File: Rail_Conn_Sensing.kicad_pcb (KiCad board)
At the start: 2 copper layers, 29 parts, among them J1 Rail Sensing Inputs, J2 Vin & GND, J3 Outputs, U1 AMC1200, U2 AMC1200, U3 MCP6004, U4 74LS00, U5 74LS86, U6 L7805

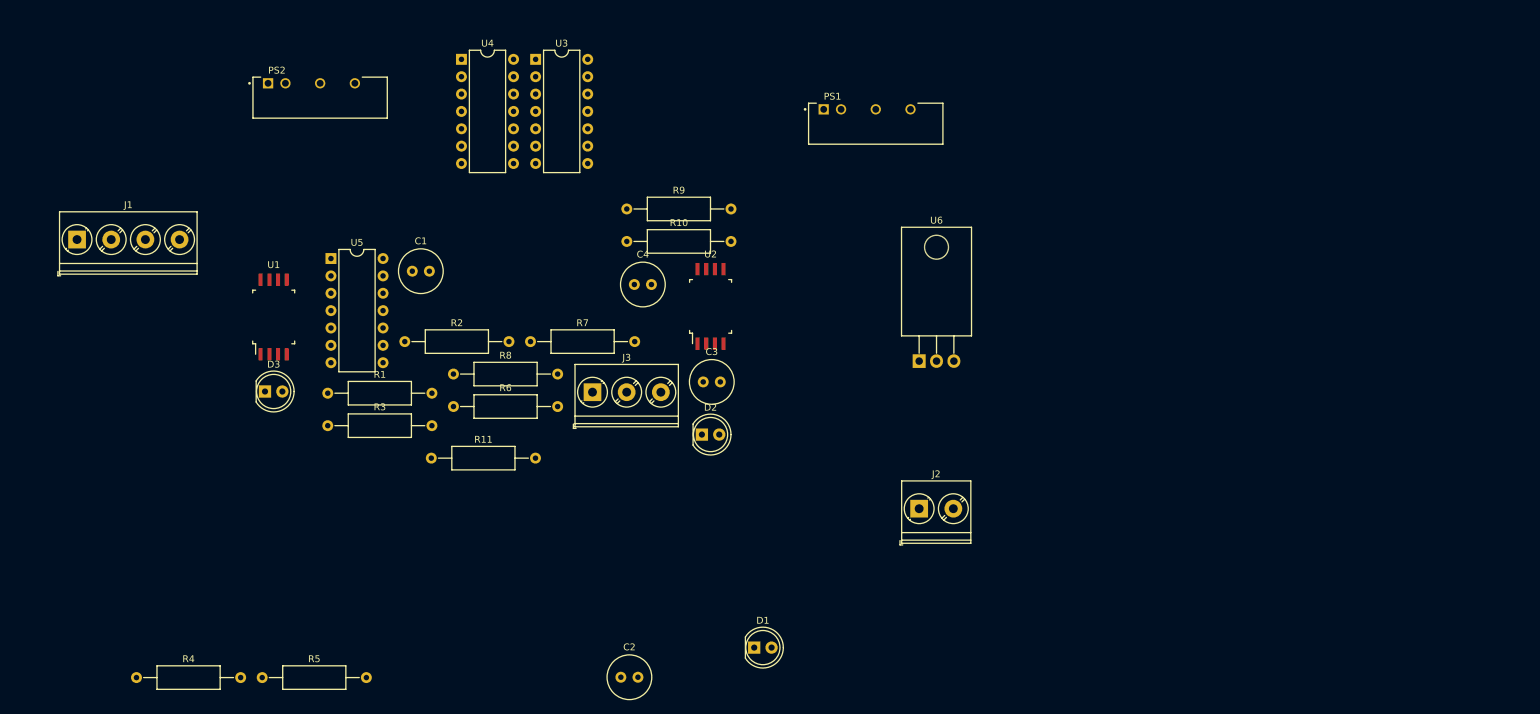
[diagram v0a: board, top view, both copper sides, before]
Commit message: Modified pcb layout
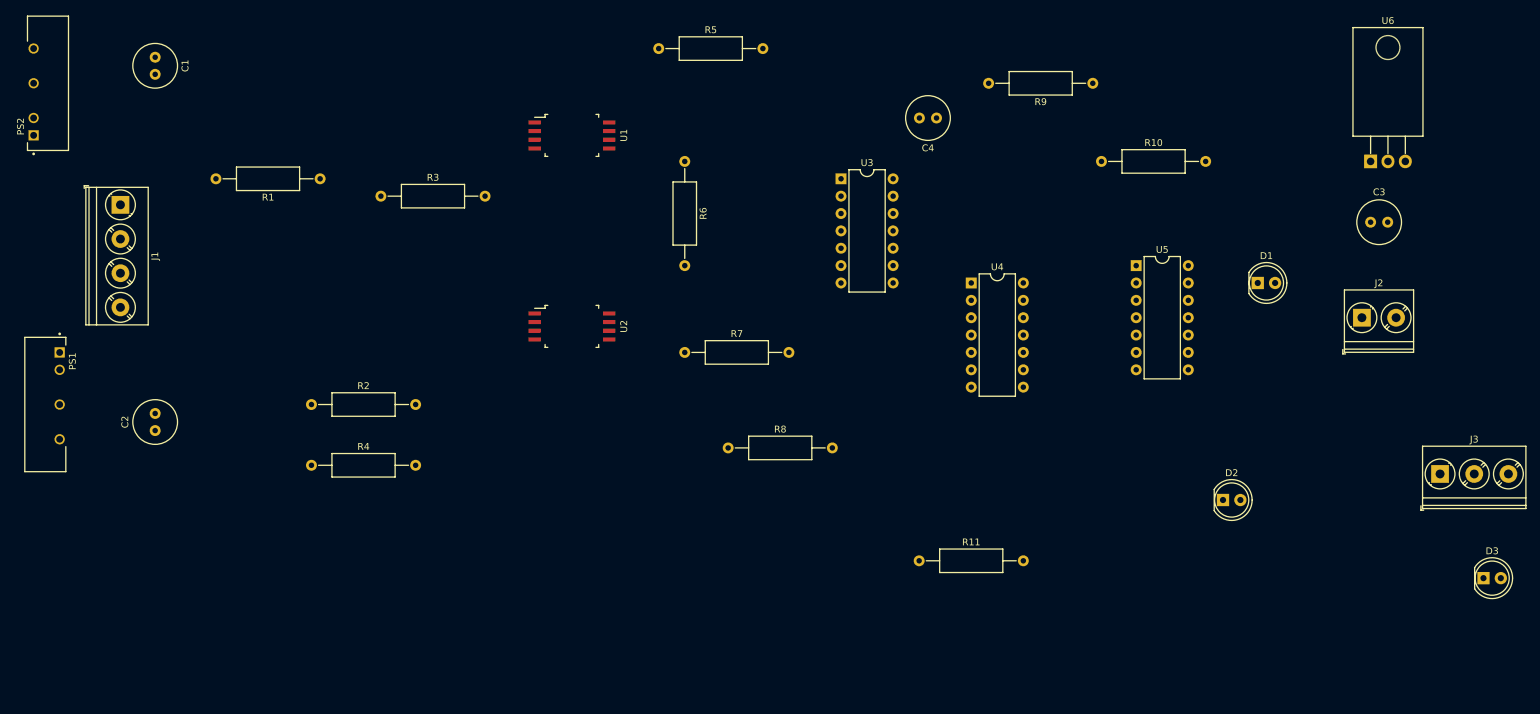
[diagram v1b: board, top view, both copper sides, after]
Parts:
- moved D3 180.3 mm to (227.3, 104.1)
- moved PS1 126.9 mm to (19.1, 78.7), turned to 270 degrees
- moved J3 124.6 mm to (221.0, 88.9)
- moved U5 117.8 mm to (176.5, 58.4)
- moved R5 108.8 mm to (106.7, 26.7)
- moved C3 100.4 mm to (210.8, 52.1)
- moved D1 90.9 mm to (194.3, 61.0)
- moved U4 81.4 mm to (152.4, 61.0)
- moved C2 77.1 mm to (33.0, 82.5), turned to 90 degrees
- moved D2 76.8 mm to (189.2, 92.7)
- moved R11 72.9 mm to (144.8, 101.6)
- moved U6 72.2 mm to (210.8, 43.2)
- moved R9 70.6 mm to (170.2, 31.8), turned to 180 degrees
- moved J2 70.5 mm to (209.6, 66.0)
- moved R10 70.4 mm to (171.4, 43.2)
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
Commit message: Modify placement of parts on PCB
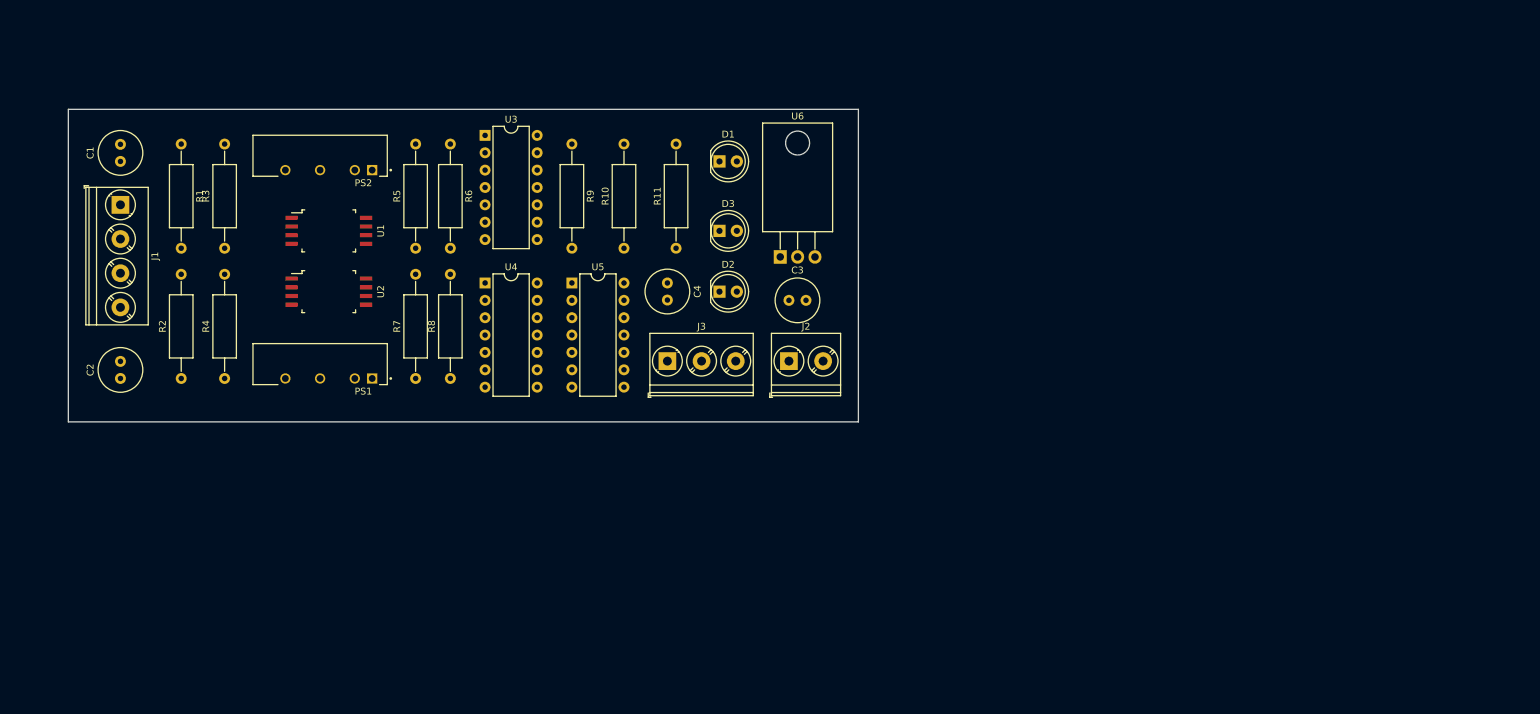
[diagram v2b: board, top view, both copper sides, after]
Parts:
- moved D3 122.8 mm to (115.6, 53.3)
- moved J3 114.2 mm to (108.0, 72.4)
- moved U6 87.5 mm to (124.5, 57.1)
- moved C3 85.9 mm to (125.7, 63.5)
- moved J2 84.1 mm to (125.7, 72.4)
- moved U5 82.6 mm to (94.0, 61.0)
- moved D1 80.7 mm to (115.6, 43.2)
- moved D2 79.7 mm to (115.6, 62.2)
- moved R9 76.7 mm to (94.0, 40.6), turned to 270 degrees
- moved U4 71.1 mm to (81.3, 61.0)
- moved R10 71.0 mm to (101.6, 55.9), turned to 90 degrees
- moved R11 57.9 mm to (109.2, 55.9), turned to 90 degrees
- moved U3 52.5 mm to (81.3, 39.4)
- moved C4 46.2 mm to (108.0, 61.0), turned to 270 degrees
- moved R5 46.0 mm to (71.1, 55.9), turned to 90 degrees
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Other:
- board outline added: 115.6 x 45.7 mm
- net class Default: clearance 0.2 -> 0.2032; trace_width 0.25 -> 0.2032; via_dia 0.8 -> 0.762; via_drill 0.4 -> 0.381
- net class Power added: clearance 0.3048, trace_width 0.3048, via_dia 0.762, via_drill 0.381
- rule pad_to_mask_clearance: 0.051 -> 0.0508
- rule solder_mask_min_width: 0.25 -> 0.1016
- rule trace_clearance: 0.2 -> 0.2032
- rule trace_min: 0.2 -> 0.2032
- rule via_min_drill: 0.3 -> 0.254
- rule via_min_size: 0.4 -> 0.508

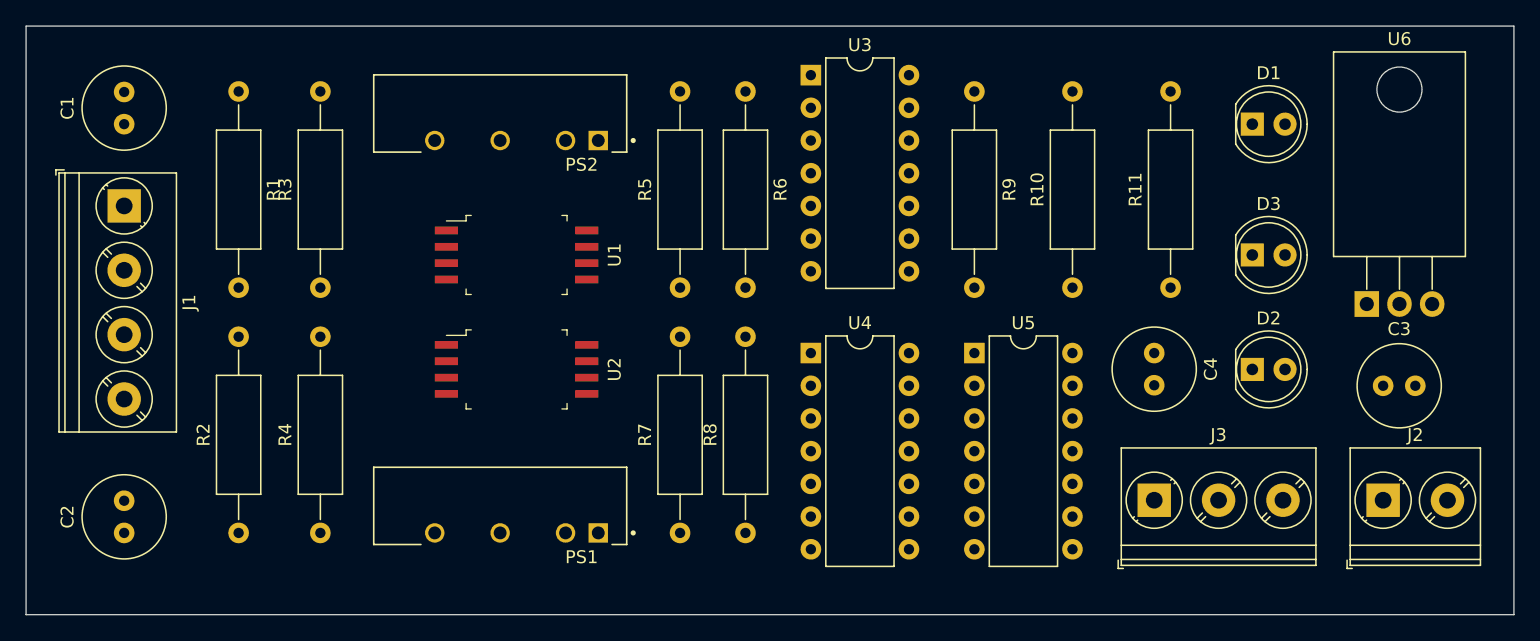
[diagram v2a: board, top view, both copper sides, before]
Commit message: Delete extra resistor divider and re-arrange pcb
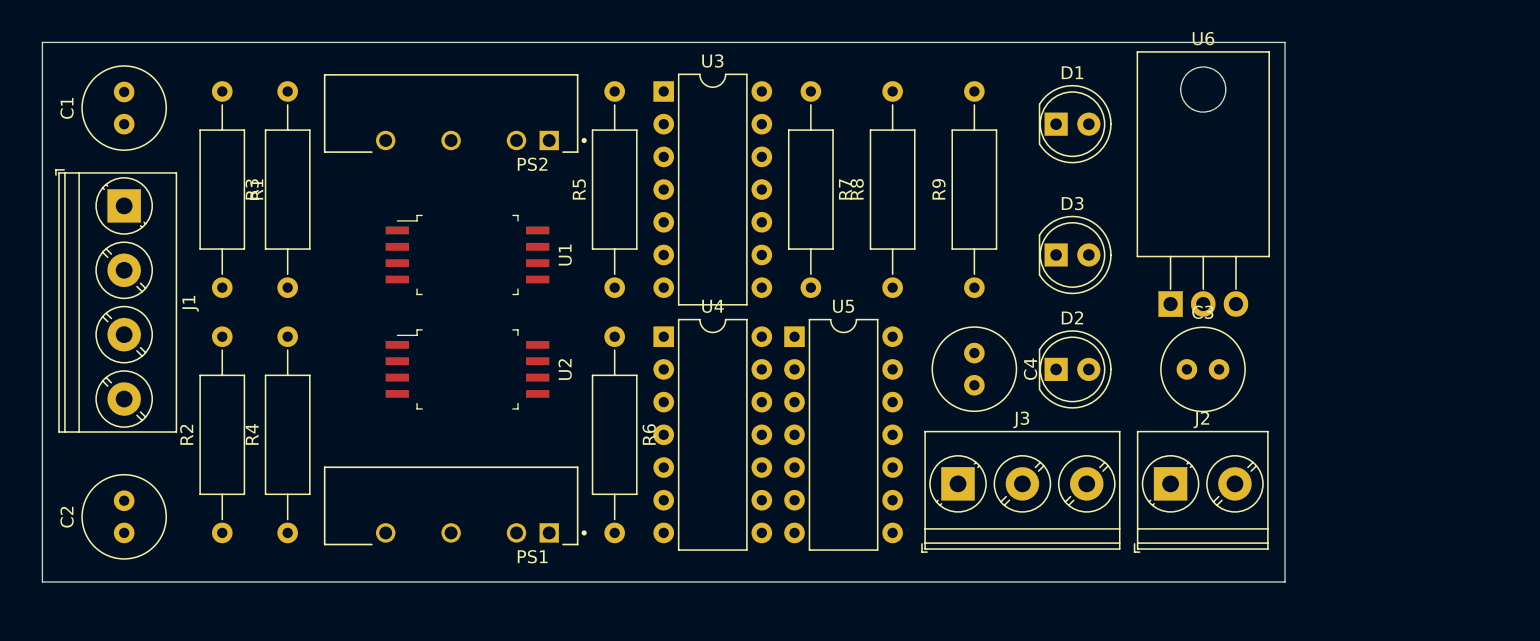
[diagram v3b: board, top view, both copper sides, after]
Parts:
- removed the R7 at (71.1, 74.9)
- removed the R8 at (76.2, 74.9)
- moved R6 21.6 mm to (66.0, 59.7)
- moved J2 16.6 mm to (109.2, 71.1)
- moved C3 15.3 mm to (110.5, 62.2)
- moved J3 15.3 mm to (92.7, 71.1)
- moved D1 15.2 mm to (100.3, 43.2)
- moved D2 15.2 mm to (100.3, 62.2)
- moved D3 15.2 mm to (100.3, 53.3)
- moved R9 15.2 mm to (94.0, 55.9)
- moved U6 15.2 mm to (109.2, 57.1)
- moved U5 14.0 mm to (80.0, 59.7)
- moved C4 14.0 mm to (94.0, 61.0)
- moved R8 14.0 mm to (87.6, 55.9)
- moved R7 12.7 mm to (81.3, 40.6)
- moved U3 11.5 mm to (69.8, 40.6)
- moved U4 11.5 mm to (69.8, 59.7)
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- renumbered R9 to R7, R10 to R8, R11 to R9
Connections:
- U3 pad 13: Net-(R7-Pad2) -> Net-(R5-Pad2)
- U3 pad 9: Net-(R7-Pad2) -> Net-(R5-Pad2)
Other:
- board size 115.6 x 45.7 mm -> 96.5 x 41.9 mm

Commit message: Add power traces to pcb
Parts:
- moved D3 2.84 mm to (102.9, 52.1), turned to 180 degrees
- moved D2 2.84 mm to (102.9, 61.0), turned to 180 degrees
- moved D1 2.54 mm to (102.9, 43.2), turned to 180 degrees
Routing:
- net +5V: track 0.00 -> 155.5 mm
- net Net-(C1-Pad2): track 0.00 -> 63.9 mm
- net Net-(C2-Pad2): track 0.00 -> 58.6 mm
- net Net-(C3-Pad1): track 0.00 -> 15.0 mm

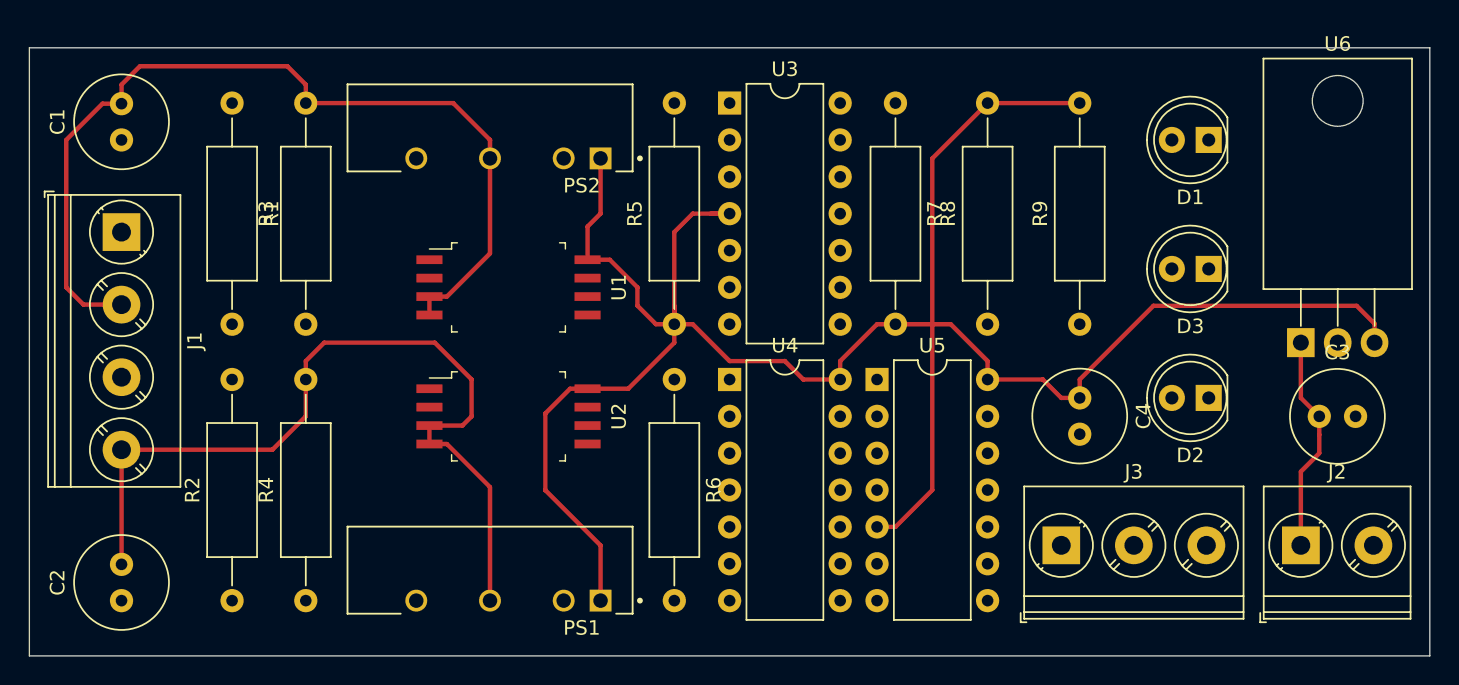
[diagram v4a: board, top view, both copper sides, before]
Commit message: Add signal wires and ground fill for pcb
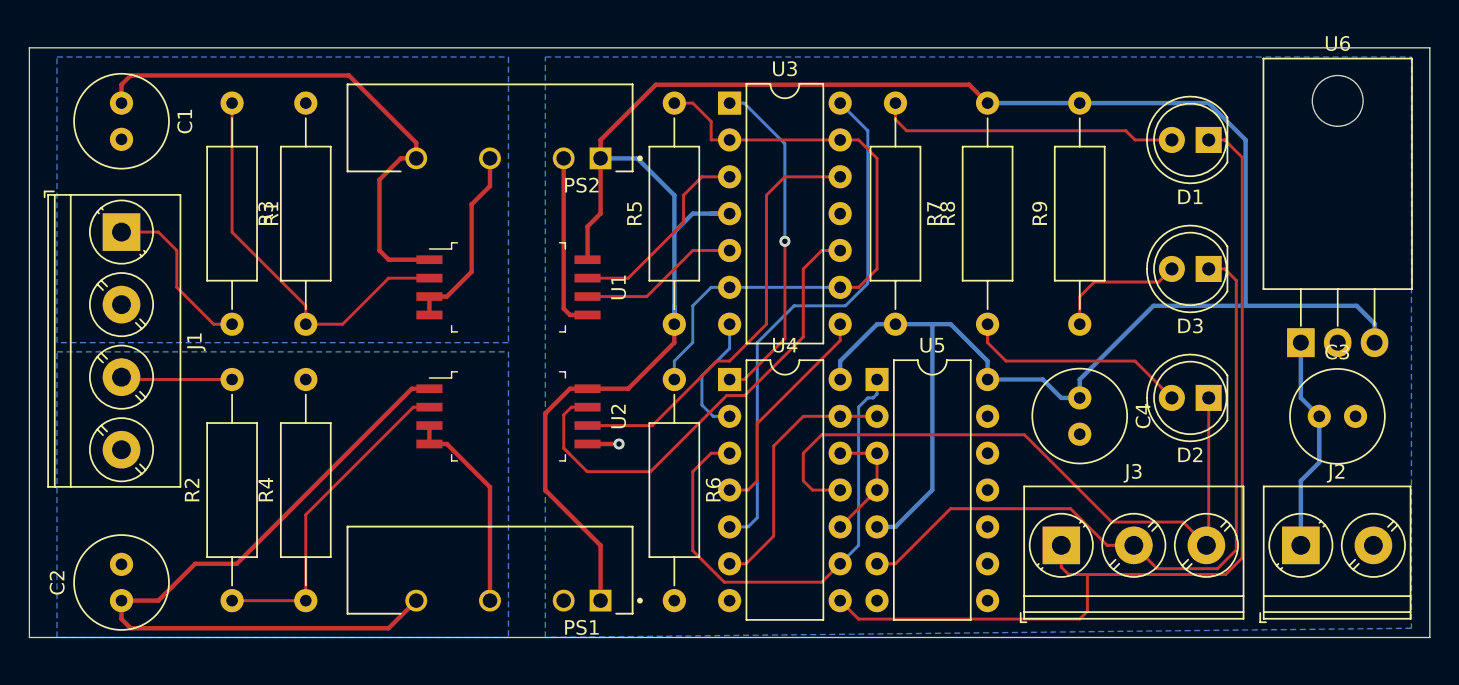
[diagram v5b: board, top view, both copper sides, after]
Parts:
- moved C1 2.54 mm to (27.9, 40.6), turned to 270 degrees
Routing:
- net Net-(D1-Pad1): track 0.00 -> 65.4 mm
- net Net-(C1-Pad2): track 63.9 -> 13.2 mm
- net Net-(C2-Pad1): track 0.00 -> 50.5 mm
- net Net-(D3-Pad1): track 0.00 -> 49.4 mm
- net Net-(D2-Pad1): track 0.00 -> 47.0 mm
- net Net-(C2-Pad2): track 58.6 -> 14.5 mm
- net Net-(R5-Pad2): track 0.00 -> 43.3 mm
- net Net-(U3-Pad14): track 0.00 -> 36.8 mm
- net Net-(C1-Pad1): track 0.00 -> 36.6 mm
- net Net-(U4-Pad3): track 0.00 -> 34.1 mm
- net Net-(U2-Pad7): track 0.00 -> 33.5 mm
- net Net-(U2-Pad6): track 0.00 -> 29.7 mm
- net Net-(R1-Pad1): track 0.00 -> 27.2 mm
- net +5V: track 155.5 -> 179.7 mm
- net Net-(U3-Pad1): track 0.00 -> 23.4 mm, vias 0 -> 1
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- added copper zone on B.Cu, net GND
- added copper zone on B.Cu, net Net-(C1-Pad2)
- added copper zone on B.Cu, net Net-(C2-Pad2)
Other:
- board size 96.5 x 41.9 mm -> 96.5 x 40.6 mm
